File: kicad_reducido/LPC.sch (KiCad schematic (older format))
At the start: 2 parts, among them J2 USB_B_Micro

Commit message: ruteado kicad reducido parcialmente completo
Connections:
- net GND: no longer LPC1.1
- net P0.2: no longer names the net of LPC1.21
- net P0.21: no longer names the net of LPC1.23
- net P0.22: no longer names the net of LPC1.24
- net P0.3: no longer names the net of LPC1.22
- net P2.1: no longer names the net of LPC1.43
- net P2.2: no longer names the net of LPC1.44
- net P2.3: no longer names the net of LPC1.45
- net P2.4: no longer names the net of LPC1.46
- net P2.5: no longer names the net of LPC1.47
- net P2.6: no longer names the net of LPC1.48
- net P2.7: no longer names the net of LPC1.49
- net P2.8: no longer names the net of LPC1.50
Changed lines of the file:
@@
 	1    0    0    -1
 $EndComp
-Text HLabel 2550 1700 0    50   Input ~ 0
+Text HLabel 2200 1700 0    50   Input ~ 0
 GND
-Text HLabel 6050 1650 2    50   Input ~ 0
+Text HLabel 6050 1700 2    50   Input ~ 0
 3.3V
 Wire Wire Line
 	5500 1700 6050 1700
-Wire Wire Line
-	6050 1700 6050 1650
 Wire Wire Line
 	2800 3400 2200 3400
@@
 Text HLabel 2200 3100 0    50   Input ~ 0
 ADC0
-Wire Wire Line
-	2800 1800 2550 1800
-Text HLabel 2550 1800 0    50   Input ~ 0
+Text HLabel 2200 1800 0    50   Input ~ 0
 5V
-Wire Wire Line
-	2800 3700 2200 3700
-Wire Wire Line
-	2800 3800 2200 3800
-Wire Wire Line
-	2800 4000 2200 4000
-Wire Wire Line
-	2800 3900 2200 3900
-Wire Wire Line
-	5500 3900 5950 3900
-Wire Wire Line
-	5500 3800 5950 3800
-Wire Wire Line
-	5500 3700 5950 3700
-Wire Wire Line
-	5500 3600 5950 3600
-Wire Wire Line
-	5500 3500 5950 3500
-Wire Wire Line
-	5500 3400 5950 3400
-Wire Wire Line
-	5500 3200 5950 3200
-Wire Wire Line
-	5500 3300 5950 3300
-Text HLabel 5950 3200 2    50   Input ~ 0
-P2.1
-Text HLabel 5950 3300 2    50   Input ~ 0
-P2.2
-Text HLabel 5950 3400 2    50   Input ~ 0
-P2.3
-Text HLabel 5950 3500 2    50   Input ~ 0
-P2.4
-Text HLabel 5950 3600 2    50   Input ~ 0
-P2.5
-Text HLabel 5950 3800 2    50   Input ~ 0
-P2.7
-Text HLabel 5950 3700 2    50   Input ~ 0
-P2.6
-Text HLabel 5950 3900 2    50   Input ~ 0
-P2.8
-Text HLabel 2200 3700 0    50   Input ~ 0
-P0.2
-Text HLabel 2200 3800 0    50   Input ~ 0
-P0.3
-Text HLabel 2200 3900 0    50   Input ~ 0
-P0.21
-Text HLabel 2200 4000 0    50   Input ~ 0
-P0.22
 $Comp
 L potenciostato-rescue:GND-power #PWR0131
@@
 	1    0    0    -1
 $EndComp
-Wire Wire Line
-	2550 1700 2650 1700
 $Comp
 L potenciostato-rescue:GND-power #PWR0132
@@
 Wire Wire Line
 	2650 1400 2650 1700
-Connection ~ 2650 1700
-Wire Wire Line
-	2650 1700 2800 1700
 Wire Wire Line
 	6950 2200 6950 2050
@@
 Text Label 4200 3950 0    50   ~ 0
 Pin12_U8
+Wire Wire Line
+	2200 1700 2650 1700
+Wire Wire Line
+	2200 1800 2800 1800
 $EndSCHEMATC

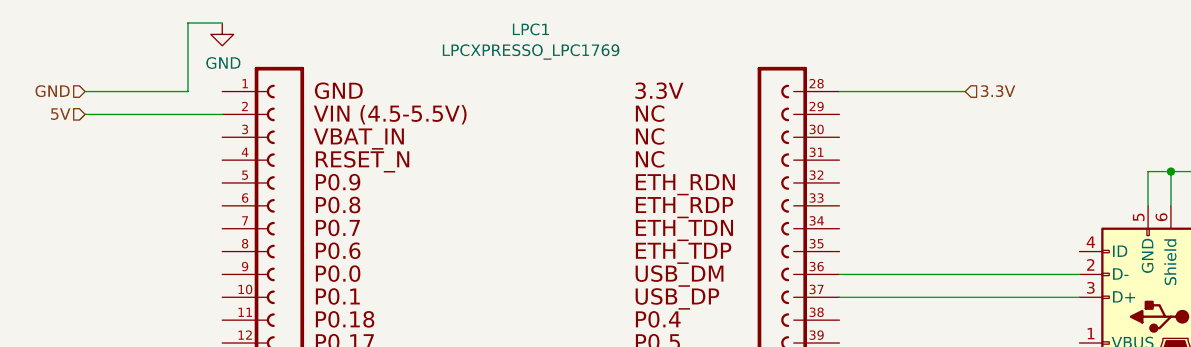
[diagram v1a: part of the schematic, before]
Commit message: pcb reducido en 10x10
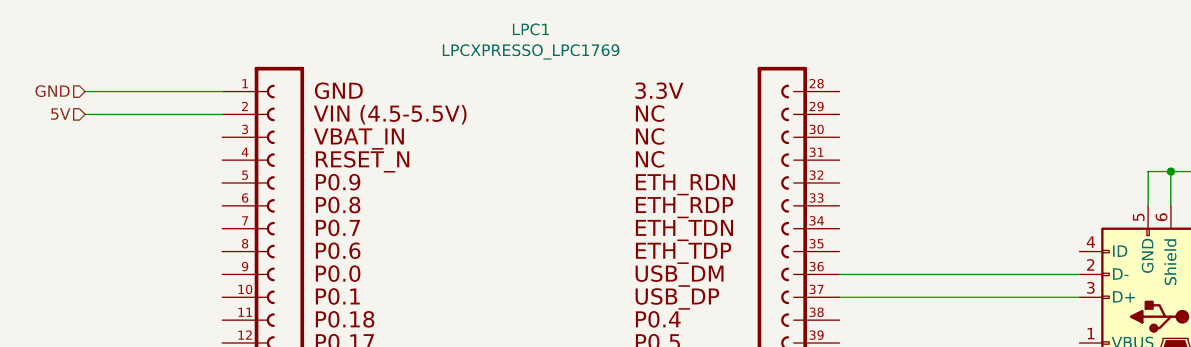
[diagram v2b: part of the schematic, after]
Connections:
- net GND: now also LPC1.1
- net 3.3V: no longer names the net of LPC1.28
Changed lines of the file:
@@
 Text HLabel 2200 1700 0    50   Input ~ 0
 GND
-Text HLabel 6050 1700 2    50   Input ~ 0
-3.3V
-Wire Wire Line
-	5500 1700 6050 1700
 Wire Wire Line
 	2800 3400 2200 3400
@@
 	1    0    0    -1
 $EndComp
-$Comp
-L potenciostato-rescue:GND-power #PWR0133
-U 1 1 60A0D30E
-P 2800 1400
-F 0 "#PWR0133" H 2800 1150 50  0001 C CNN
-F 1 "GND" H 2805 1223 50  0000 C CNN
-F 2 "" H 2800 1400 50  0001 C CNN
-F 3 "" H 2800 1400 50  0001 C CNN
-	1    2800 1400
-	1    0    0    -1
-$EndComp
-Wire Wire Line
-	2800 1400 2650 1400
-Wire Wire Line
-	2650 1400 2650 1700
 Wire Wire Line
 	6950 2200 6950 2050
@@
 Pin12_U8
 Wire Wire Line
-	2200 1700 2650 1700
+	2200 1800 2800 1800
 Wire Wire Line
-	2200 1800 2800 1800
+	2200 1700 2800 1700
 $EndSCHEMATC

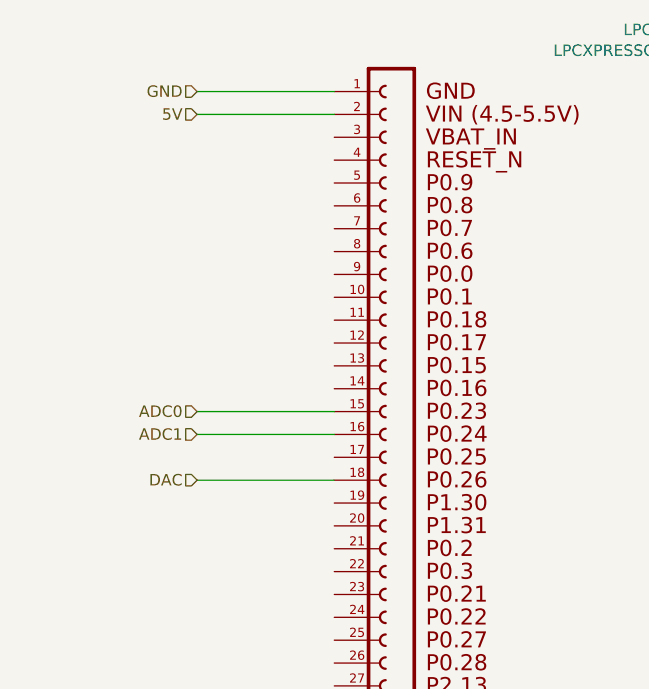
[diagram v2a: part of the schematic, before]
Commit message: pcb reducido listo falta revisar
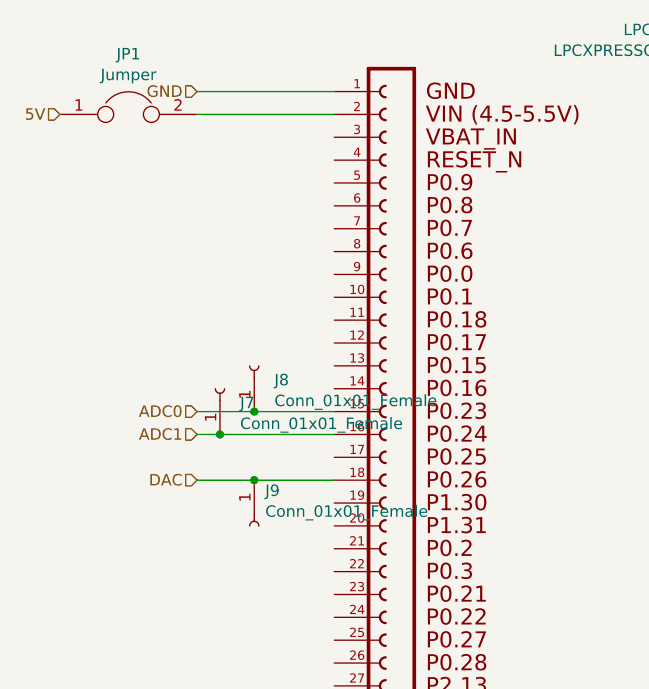
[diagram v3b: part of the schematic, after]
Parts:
- added J7, J8, J9: Conn_01x01_Female, Connector_PinHeader_2.54mm:PinHeader_1x01_P2.54mm_Vertical, symbol Connector:Conn_01x01_Female
- added JP1: Jumper, Connector_PinHeader_2.54mm:PinHeader_1x02_P2.54mm_Vertical, symbol Device:Jumper
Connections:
- net 5V: now also JP1.1; no longer LPC1.2
- net ADC0: now also J8.1 (Pin_1)
- net ADC1: now also J7.1 (Pin_1)
- net DAC: now also J9.1 (Pin_1)
- new net: JP1.2, LPC1.2
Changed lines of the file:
@@
 GND
 Wire Wire Line
-	2800 3400 2200 3400
+	2800 3400 2450 3400
 Text HLabel 2200 3400 0    50   Input ~ 0
 DAC
@@
 	6850 2050 6850 2200
 Wire Wire Line
-	2800 3100 2200 3100
+	2800 3100 2450 3100
 Wire Wire Line
-	2800 3200 2200 3200
+	2800 3200 2300 3200
 Text HLabel 2200 3200 0    50   Input ~ 0
 ADC1
 Text HLabel 2200 3100 0    50   Input ~ 0
 ADC0
-Text HLabel 2200 1800 0    50   Input ~ 0
+Text HLabel 1600 1800 0    50   Input ~ 0
 5V
 $Comp
@@
 Wire Wire Line
 	2200 1700 2800 1700
+$Comp
+L Device:Jumper JP1
+U 1 1 6184E96B
+P 1900 1800
+F 0 "JP1" H 1900 2064 50  0000 C CNN
+F 1 "Jumper" H 1900 1973 50  0000 C CNN
+F 2 "Connector_PinHeader_2.54mm:PinHeader_1x02_P2.54mm_Vertical" H 1900 1800 50  0001 C CNN
+F 3 "~" H 1900 1800 50  0001 C CNN
+	1    1900 1800
+	1    0    0    -1
+$EndComp
+$Comp
+L Connector:Conn_01x01_Female J8
+U 1 1 6184FD8B
+P 2450 2900
+F 0 "J8" V 2388 2812 50  0000 R CNN
+F 1 "Conn_01x01_Female" V 2297 2812 50  0000 R CNN
+F 2 "Connector_PinHeader_2.54mm:PinHeader_1x01_P2.54mm_Vertical" H 2450 2900 50  0001 C CNN
+F 3 "~" H 2450 2900 50  0001 C CNN
+	1    2450 2900
+	0    -1   -1   0
+$EndComp
+Connection ~ 2450 3100
+Wire Wire Line
+	2450 3100 2200 3100
+$Comp
+L Connector:Conn_01x01_Female J9
+U 1 1 618507D3
+P 2450 3600
+F 0 "J9" V 2296 3648 50  0000 L CNN
+F 1 "Conn_01x01_Female" V 2387 3648 50  0000 L CNN
+F 2 "Connector_PinHeader_2.54mm:PinHeader_1x01_P2.54mm_Vertical" H 2450 3600 50  0001 C CNN
+F 3 "~" H 2450 3600 50  0001 C CNN
+	1    2450 3600
+	0    1    1    0
+$EndComp
+Connection ~ 2450 3400
+Wire Wire Line
+	2450 3400 2200 3400
+$Comp
+L Connector:Conn_01x01_Female J7
+U 1 1 61850C4C
+P 2300 3000
+F 0 "J7" V 2238 2912 50  0000 R CNN
+F 1 "Conn_01x01_Female" V 2147 2912 50  0000 R CNN
+F 2 "Connector_PinHeader_2.54mm:PinHeader_1x01_P2.54mm_Vertical" H 2300 3000 50  0001 C CNN
+F 3 "~" H 2300 3000 50  0001 C CNN
+	1    2300 3000
+	0    -1   -1   0
+$EndComp
+Connection ~ 2300 3200
+Wire Wire Line
+	2300 3200 2200 3200
 $EndSCHEMATC

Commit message: agregado lo de Hernan y fixeado el kicad pcb
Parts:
- renumbered J8 to J10, J9 to J11, J2 to J12, J7 to J9
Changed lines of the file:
@@
 DAC
 $Comp
-L potenciostato-rescue:USB_B_Micro-Connector J2
+L potenciostato-rescue:USB_B_Micro-Connector J?
 U 1 1 609A40C2
 P 6850 2600
-AR Path="/609A40C2" Ref="J2"  Part="1"
-AR Path="/60147E53/609A40C2" Ref="J2"  Part="1"
-F 0 "J2" H 6620 2496 50  0000 R CNN
+AR Path="/609A40C2" Ref="J?"  Part="1"
+AR Path="/60147E53/609A40C2" Ref="J12"  Part="1"
+F 0 "J12" H 6620 2496 50  0000 R CNN
 F 1 "USB_B_Micro" H 6620 2589 50  0000 R CNN
 F 2 "Connector_USB:USB_Mini-B_Wuerth_65100516121_Horizontal" H 7000 2550 50  0001 C CNN
@@
 5V
 $Comp
-L potenciostato-rescue:GND-power #PWR0131
+L potenciostato-rescue:GND-power #PWR017
 U 1 1 60A0C4F1
 P 5700 4300
-F 0 "#PWR0131" H 5700 4050 50  0001 C CNN
+F 0 "#PWR017" H 5700 4050 50  0001 C CNN
 F 1 "GND" H 5705 4123 50  0000 C CNN
 F 2 "" H 5700 4300 50  0001 C CNN
@@
 $EndComp
 $Comp
-L potenciostato-rescue:GND-power #PWR0132
+L potenciostato-rescue:GND-power #PWR018
 U 1 1 60A0D2ED
 P 7400 2050
-F 0 "#PWR0132" H 7400 1800 50  0001 C CNN
+F 0 "#PWR018" H 7400 1800 50  0001 C CNN
 F 1 "GND" H 7405 1873 50  0000 C CNN
 F 2 "" H 7400 2050 50  0001 C CNN
@@
 $EndComp
 $Comp
-L Connector:Conn_01x01_Female J8
+L Connector:Conn_01x01_Female J10
 U 1 1 6184FD8B
 P 2450 2900
-F 0 "J8" V 2388 2812 50  0000 R CNN
+F 0 "J10" V 2388 2812 50  0000 R CNN
 F 1 "Conn_01x01_Female" V 2297 2812 50  0000 R CNN
 F 2 "Connector_PinHeader_2.54mm:PinHeader_1x01_P2.54mm_Vertical" H 2450 2900 50  0001 C CNN
@@
 	2450 3100 2200 3100
 $Comp
-L Connector:Conn_01x01_Female J9
+L Connector:Conn_01x01_Female J11
 U 1 1 618507D3
 P 2450 3600
-F 0 "J9" V 2296 3648 50  0000 L CNN
+F 0 "J11" V 2296 3648 50  0000 L CNN
 F 1 "Conn_01x01_Female" V 2387 3648 50  0000 L CNN
 F 2 "Connector_PinHeader_2.54mm:PinHeader_1x01_P2.54mm_Vertical" H 2450 3600 50  0001 C CNN
@@
 	2450 3400 2200 3400
 $Comp
-L Connector:Conn_01x01_Female J7
+L Connector:Conn_01x01_Female J9
 U 1 1 61850C4C
 P 2300 3000
-F 0 "J7" V 2238 2912 50  0000 R CNN
+F 0 "J9" V 2238 2912 50  0000 R CNN
 F 1 "Conn_01x01_Female" V 2147 2912 50  0000 R CNN
 F 2 "Connector_PinHeader_2.54mm:PinHeader_1x01_P2.54mm_Vertical" H 2300 3000 50  0001 C CNN
